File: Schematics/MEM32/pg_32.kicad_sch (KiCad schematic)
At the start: 18 parts

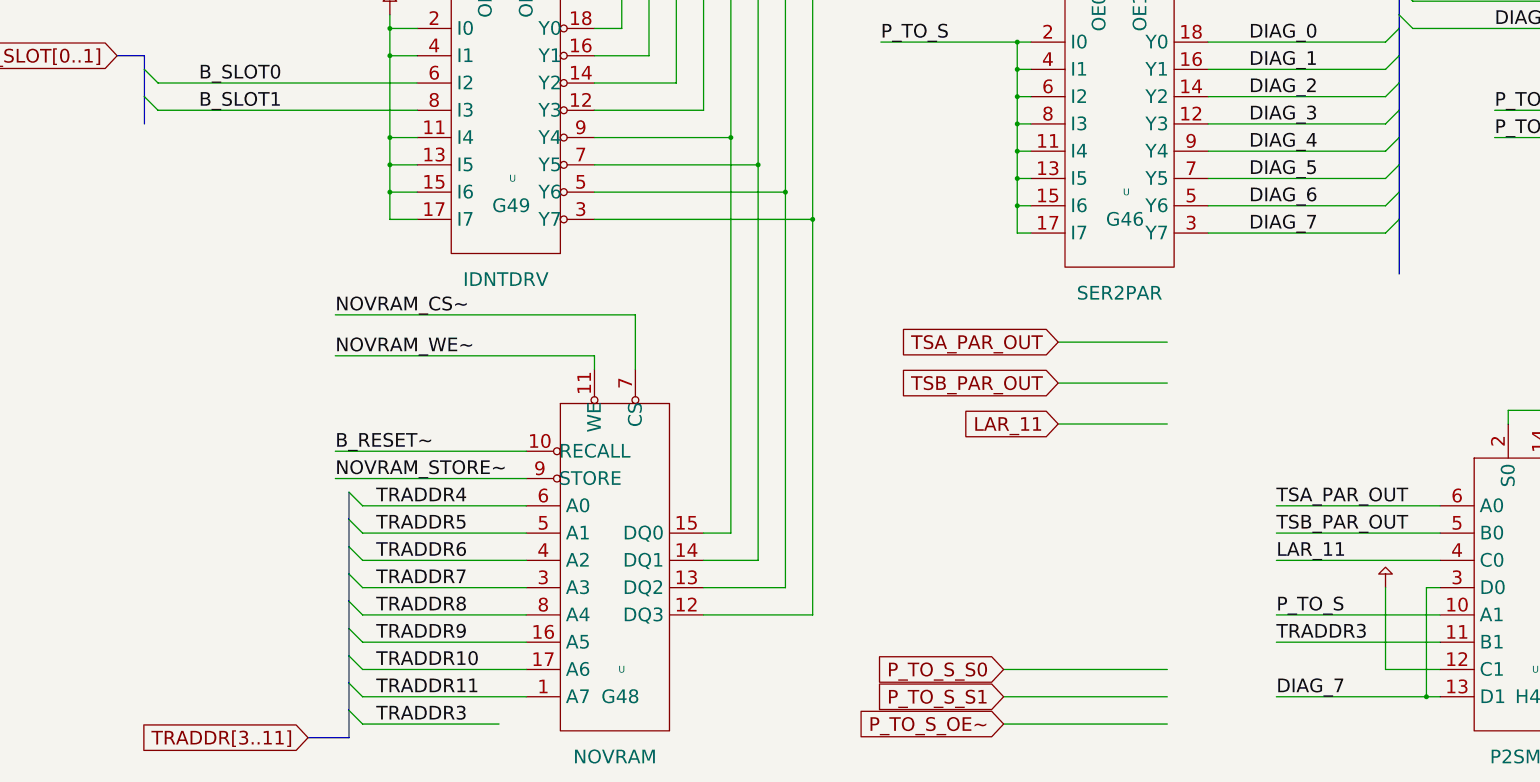
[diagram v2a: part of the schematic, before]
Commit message: MEM32: Prune trace hardware.  Tested to 2.43 seconds
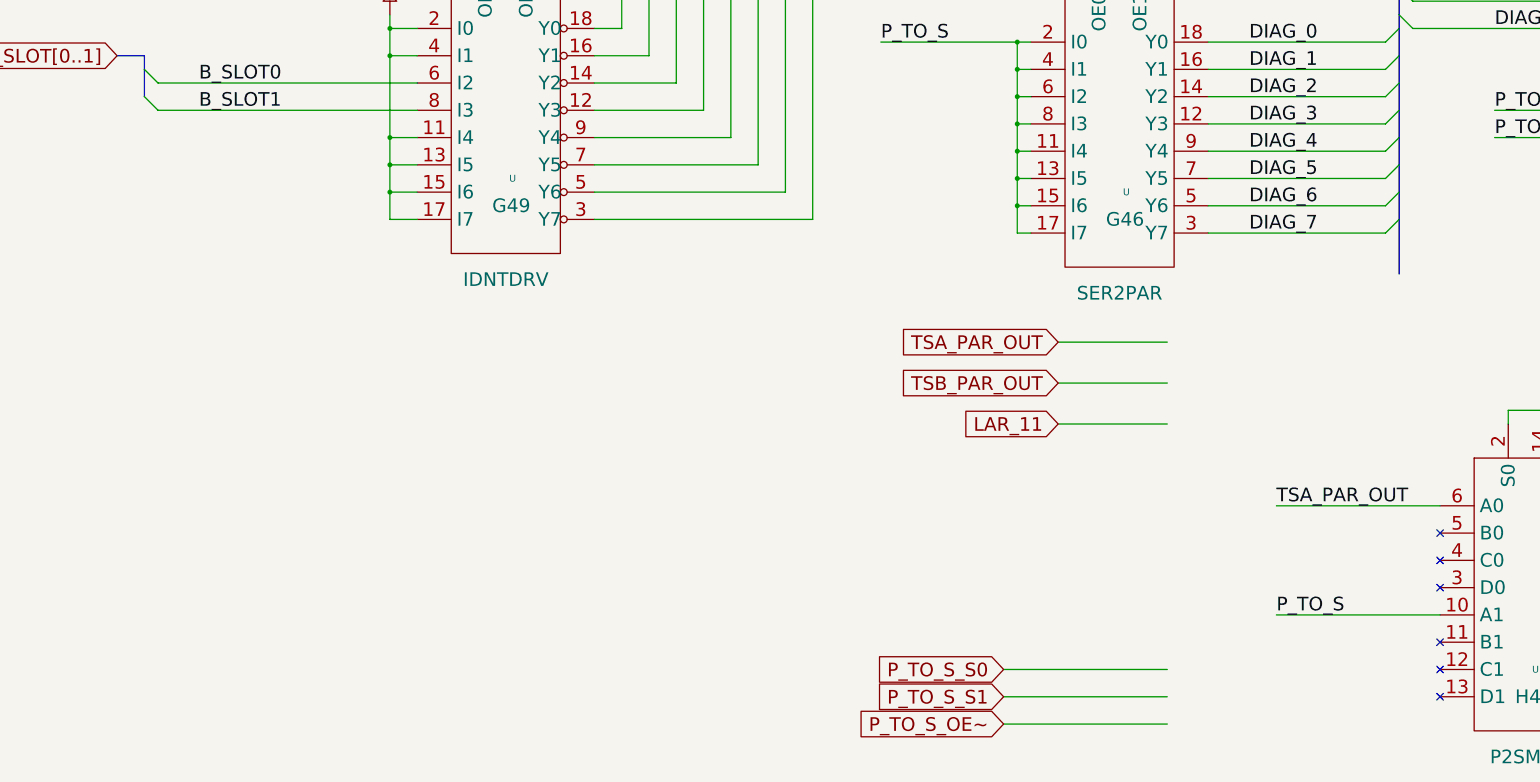
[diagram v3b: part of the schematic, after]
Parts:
- removed U: (no value), symbol r1000:NOVRAM
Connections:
- net DIAG_7: no longer U.13 (D1), U.3 (D0)
- net LAR_11: no longer U.4 (C0)
- net PU: no longer U.12 (C1)
- net TSB_PAR_OUT: no longer U.5 (B0)
- net TRADDR3: no longer names the net of U.11 (B1)
- no-connect marks 12 -> 18

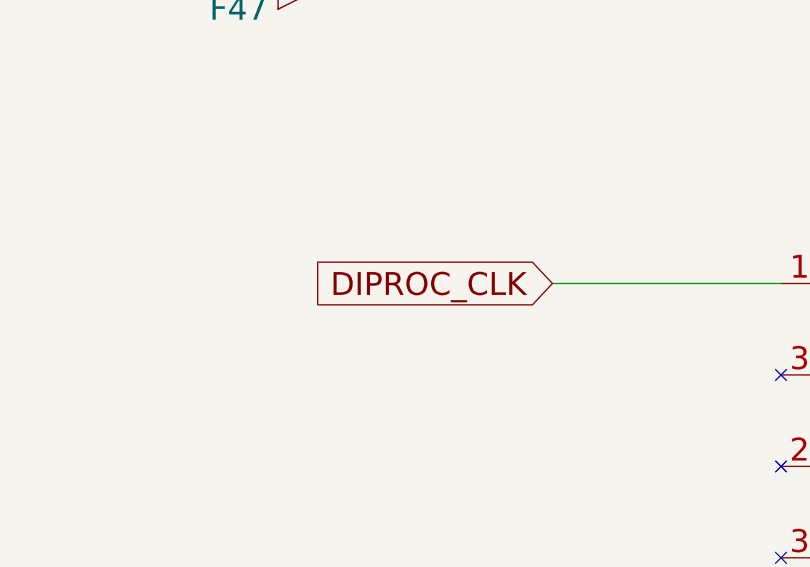
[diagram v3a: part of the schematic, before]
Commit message: MEM32: polish, tested to 9.80 seconds (rc042)
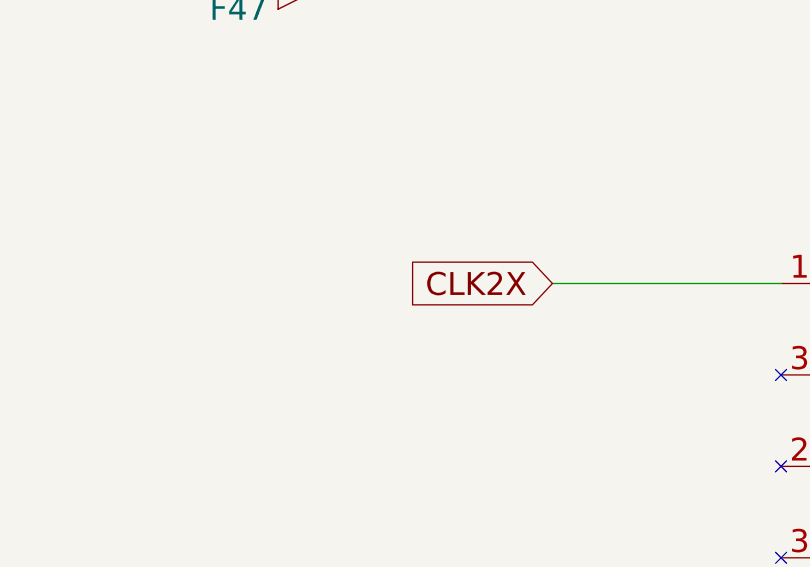
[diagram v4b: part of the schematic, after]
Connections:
- net DIPROC_CLK is gone; now on net CLK2X: U.18 (XTAL2)
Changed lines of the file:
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@@
     )
   )
-  (global_label "DIPROC_CLK" (shape input) (at 104.14 76.2 180) (fields_autoplaced)
+  (global_label "CLK2X" (shape input) (at 104.14 76.2 180) (fields_autoplaced)
     (effects (font (size 2.54 2.54)) (justify right))
     (property "Intersheet References" "${INTERSHEET_REFS}" (id 0) (at 76.4026 76.0413 0)

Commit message: MEM32: Polish. tested to 5.5s (rc059)
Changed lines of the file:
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@@
-    (stroke (width 0) (type default))
-  )
-  (wire (pts (xy 297.18 299.72) (xy 317.5 299.72))
     (stroke (width 0) (type default))
   )
@@
   )
   (wire (pts (xy 444.5 83.82) (xy 444.5 106.68))
-    (stroke (width 0) (type default))
-  )
-  (bus (pts (xy 360.68 261.62) (xy 360.68 271.78))
     (stroke (width 0) (type default))
   )
@@
     )
   )
-  (global_label "LAR_11" (shape input) (at 297.18 299.72 180) (fields_autoplaced)
-    (effects (font (size 2.54 2.54)) (justify right))
-    (property "Intersheet References" "${INTERSHEET_REFS}" (id 0) (at 278.9978 299.5613 0)
-      (effects (font (size 1.905 1.905)) (justify right))
-    )
-  )

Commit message: MEM32: major polish.  tested to 30 seconds (rc059)
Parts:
- removed U: (no value), symbol r1000:F153
- removed U: (no value), symbol r1000:F299
- removed U: (no value), symbol r1000:F244
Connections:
- no-connect marks 18 -> 11
